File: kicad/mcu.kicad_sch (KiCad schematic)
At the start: 38 parts, among them J301 Debug, J302 Conn_01x03_Pin, Q303 2N7002, SW301 SW_Push, U301 W25Q16JVSS, U302 RP2040, U303 AP22804AW5, Y301 12Mhz

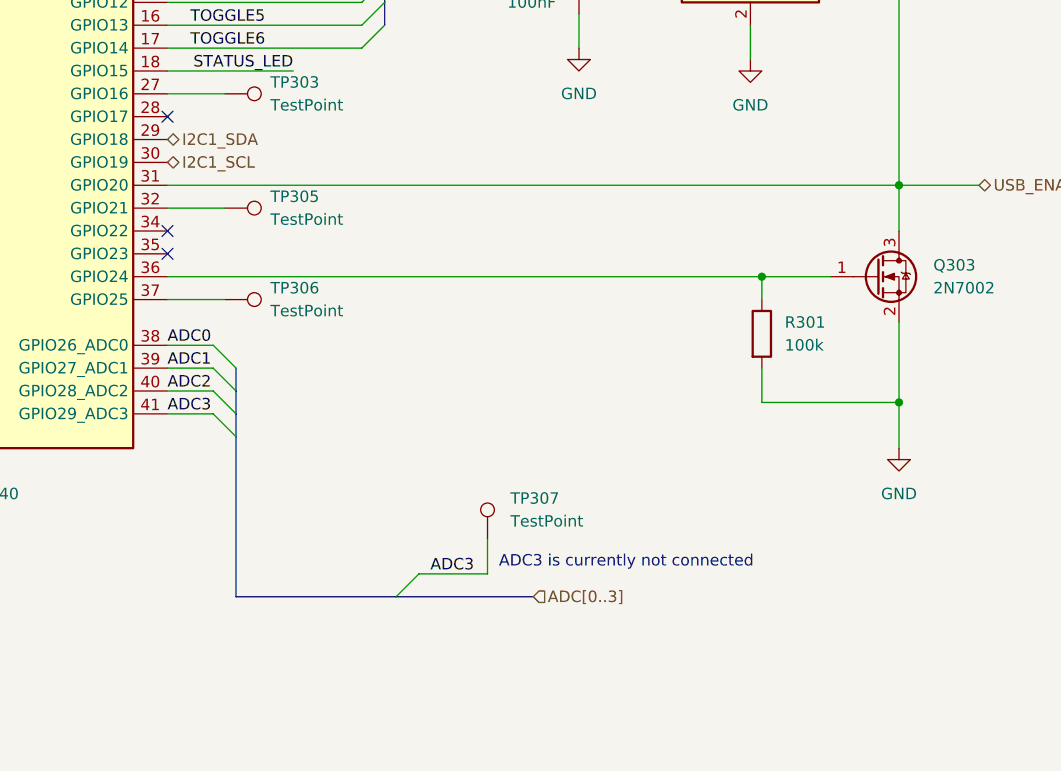
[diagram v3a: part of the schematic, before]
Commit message: Add check for DRC
Only checking errors at the moment, as the board is not ready yet
Moved unconnected Items to severity warning.
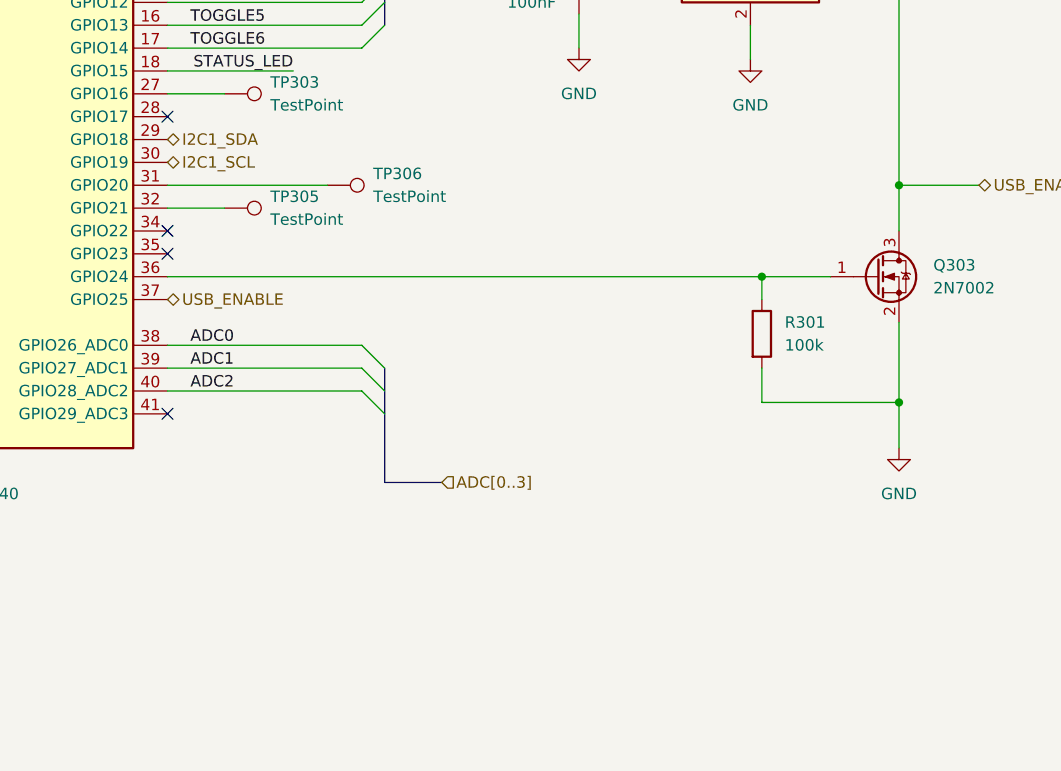
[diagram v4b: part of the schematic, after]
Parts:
- removed TP307: TestPoint, Connector_PinHeader_2.54mm:PinHeader_1x01_P2.54mm_Vertical, symbol Connector:TestPoint
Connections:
- net USB_ENABLE: now also U302.37 (GPIO25); no longer U302.31 (GPIO20)
- net at TP306.1: now also U302.31 (GPIO20); no longer U302.37 (GPIO25)
- net ADC3: no longer names the net of U302.41 (GPIO29_ADC3)
- no-connect marks 7 -> 8
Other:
- note removed: "ADC3 is currently not connected"
- moved on the sheet: TP306
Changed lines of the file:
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@@
 	)
 	(no_connect
+		(at 176.53 132.08)
+	)
+	(no_connect
 		(at 176.53 114.3)
 	)
@@
 	)
 	(bus_entry
-		(at 184.15 129.54)
-		(size -2.54 -2.54)
-		(stroke
-			(width 0)
-			(type default)
-		)
-	)
-	(bus_entry
-		(at 184.15 134.62)
+		(at 200.66 129.54)
 		(size -2.54 -2.54)
 		(stroke
@@
 	)
 	(bus_entry
-		(at 201.93 152.4)
-		(size 2.54 -2.54)
-		(stroke
-			(width 0)
-			(type default)
-		)
-	)
-	(bus_entry
 		(at 200.66 86.36)
 		(size -2.54 2.54)
@@
 	)
 	(bus_entry
-		(at 184.15 132.08)
+		(at 200.66 132.08)
 		(size -2.54 -2.54)
 		(stroke
@@
 	)
 	(bus_entry
-		(at 184.15 127)
+		(at 200.66 127)
 		(size -2.54 -2.54)
 		(stroke
@@
 		)
 	)
-	(bus
-		(pts
-			(xy 201.93 152.4) (xy 217.17 152.4)
-		)
-		(stroke
-			(width 0)
-			(type default)
-		)
-	)
 	(wire
 		(pts
@@
 	(bus
 		(pts
-			(xy 184.15 134.62) (xy 184.15 152.4)
+			(xy 200.66 132.08) (xy 200.66 139.7)
 		)
 		(stroke
@@
 	(wire
 		(pts
-			(xy 212.09 146.05) (xy 212.09 149.86)
+			(xy 257.81 27.94) (xy 257.81 30.48)
 		)
 		(stroke
@@
 	(wire
 		(pts
-			(xy 257.81 27.94) (xy 257.81 30.48)
+			(xy 241.3 88.9) (xy 241.3 92.71)
 		)
 		(stroke
@@
 	(wire
 		(pts
-			(xy 241.3 88.9) (xy 241.3 92.71)
+			(xy 176.53 127) (xy 198.12 127)
 		)
 		(stroke
@@
 	(wire
 		(pts
-			(xy 137.16 27.94) (xy 137.16 31.75)
+			(xy 176.53 106.68) (xy 194.31 106.68)
 		)
 		(stroke
@@
 	(wire
 		(pts
-			(xy 176.53 119.38) (xy 182.88 119.38)
+			(xy 137.16 27.94) (xy 137.16 31.75)
 		)
 		(stroke
@@
 	(bus
 		(pts
-			(xy 184.15 129.54) (xy 184.15 132.08)
+			(xy 200.66 129.54) (xy 200.66 132.08)
 		)
 		(stroke
@@
 	(bus
 		(pts
-			(xy 184.15 152.4) (xy 201.93 152.4)
+			(xy 200.66 139.7) (xy 207.01 139.7)
 		)
 		(stroke
@@
 	(wire
 		(pts
-			(xy 176.53 129.54) (xy 181.61 129.54)
-		)
-		(stroke
-			(width 0)
-			(type default)
-		)
-	)
-	(wire
-		(pts
 			(xy 232.41 20.32) (xy 219.71 20.32)
 		)
@@
 	(wire
 		(pts
+			(xy 176.53 129.54) (xy 198.12 129.54)
+		)
+		(stroke
+			(width 0)
+			(type default)
+		)
+	)
+	(wire
+		(pts
 			(xy 91.44 78.74) (xy 125.73 78.74)
 		)
@@
 	(wire
 		(pts
-			(xy 176.53 132.08) (xy 181.61 132.08)
-		)
-		(stroke
-			(width 0)
-			(type default)
-		)
-	)
-	(wire
-		(pts
 			(xy 270.51 20.32) (xy 270.51 22.86)
 		)
@@
 		)
 	)
-	(wire
+	(bus
 		(pts
-			(xy 176.53 127) (xy 181.61 127)
+			(xy 200.66 127) (xy 200.66 129.54)
 		)
 		(stroke
@@
 		)
 	)
-	(bus
+	(wire
 		(pts
-			(xy 184.15 127) (xy 184.15 129.54)
+			(xy 242.57 116.84) (xy 176.53 116.84)
 		)
 		(stroke
@@
 	(wire
 		(pts
-			(xy 242.57 116.84) (xy 176.53 116.84)
+			(xy 257.81 20.32) (xy 257.81 22.86)
 		)
 		(stroke
@@
 	(wire
 		(pts
-			(xy 257.81 20.32) (xy 257.81 22.86)
+			(xy 36.83 173.99) (xy 44.45 173.99)
 		)
 		(stroke
@@
 	(wire
 		(pts
-			(xy 36.83 173.99) (xy 44.45 173.99)
+			(xy 176.53 124.46) (xy 198.12 124.46)
 		)
 		(stroke
@@
 	(wire
 		(pts
-			(xy 204.47 149.86) (xy 212.09 149.86)
-		)
-		(stroke
-			(width 0)
-			(type default)
-		)
-	)
-	(wire
-		(pts
 			(xy 176.53 86.36) (xy 198.12 86.36)
 		)
@@
 	(wire
 		(pts
-			(xy 181.61 124.46) (xy 176.53 124.46)
-		)
-		(stroke
-			(width 0)
-			(type default)
-		)
-	)
-	(wire
-		(pts
-			(xy 176.53 106.68) (xy 257.81 106.68)
-		)
-		(stroke
-			(width 0)
-			(type default)
-		)
-	)
-	(bus
-		(pts
-			(xy 184.15 132.08) (xy 184.15 134.62)
-		)
-		(stroke
-			(width 0)
-			(type default)
-		)
-	)
-	(wire
-		(pts
 			(xy 91.44 83.82) (xy 125.73 83.82)
 		)
@@
 		)
 	)
-	(text "ADC3 is currently not connected"
-		(exclude_from_sim no)
-		(at 213.36 148.59 0)
-		(effects
-			(font
-				(size 1.27 1.27)
-			)
-			(justify left)
-		)
-	)
 	(label "SWCLK"
 		(at 44.45 173.99 180)
@@
 		)
 	)
-	(label "ADC3"
-		(at 176.53 132.08 0)
-		(fields_autoplaced yes)
-		(effects
-			(font
-				(size 1.27 1.27)
-			)
-			(justify left bottom)
-		)
-	)
 	(label "DEBUG_TX"
 		(at 142.24 176.53 180)
@@
 	)
 	(label "ADC0"
-		(at 176.53 124.46 0)
+		(at 179.07 124.46 0)
 		(fields_autoplaced yes)
 		(effects
@@
 		)
 	)
-	(label "ADC3"
-		(at 205.74 149.86 0)
-		(fields_autoplaced yes)
-		(effects
-			(font
-				(size 1.27 1.27)
-			)
-			(justify left bottom)
-		)
-	)
 	(label "USB_VDD"
 		(at 175.26 19.05 180)
@@
 	)
 	(label "ADC2"
-		(at 176.53 129.54 0)
+		(at 179.07 129.54 0)
 		(fields_autoplaced yes)
 		(effects
@@
 	)
 	(label "ADC1"
-		(at 176.53 127 0)
+		(at 179.07 127 0)
 		(fields_autoplaced yes)
 		(effects
@@
 		)
 	)
+	(hierarchical_label "USB_ENABLE"
+		(shape bidirectional)
+		(at 176.53 119.38 0)
+		(fields_autoplaced yes)
+		(effects
+			(font
+				(size 1.27 1.27)
+			)
+			(justify left)
+		)
+	)
 	(hierarchical_label "ADC[0..3]"
 		(shape input)
-		(at 217.17 152.4 0)
+		(at 207.01 139.7 0)
 		(fields_autoplaced yes)
 		(effects
@@
 	(symbol
 		(lib_id "Connector:TestPoint")
-		(at 182.88 119.38 270)
+		(at 194.31 106.68 270)
 		(unit 1)
 		(exclude_from_sim no)
@@
 		(fields_autoplaced yes)
 		(property "Reference" "TP306"
-			(at 187.96 118.1099 90)
+			(at 199.39 105.4099 90)
 			(effects
 				(font
@@
 		)
 		(property "Value" "TestPoint"
-			(at 187.96 120.6499 90)
+			(at 199.39 107.9499 90)
 			(effects
 				(font
@@
 		)
 		(property "Footprint" "Connector_PinHeader_2.54mm:PinHeader_1x01_P2.54mm_Vertical"
-			(at 182.88 124.46 0)
+			(at 194.31 111.76 0)
 			(effects
 				(font
@@
 		)
 		(property "Datasheet" "~"
-			(at 182.88 124.46 0)
+			(at 194.31 111.76 0)
 			(effects
 				(font
@@
 		)
 		(property "Description" "test point"
-			(at 182.88 119.38 0)
+			(at 194.31 106.68 0)
 			(effects
 				(font
@@
 					(unit 1)
 				)
-			)
-		)
-	)
-	(symbol
-		(lib_id "Connector:TestPoint")
-		(at 212.09 146.05 0)
-		(unit 1)
-		(exclude_from_sim no)
-		(in_bom yes)
-		(on_board yes)
-		(dnp no)
-		(fields_autoplaced yes)
-		(property "Reference" "TP307"
-			(at 214.63 141.4779 0)
-			(effects
-				(font
-					(size 1.27 1.27)
-				)
-				(justify left)
-			)
-		)
-		(property "Value" "TestPoint"
-			(at 214.63 144.0179 0)
-			(effects
-				(font
-					(size 1.27 1.27)
-				)
-				(justify left)
-			)
-		)
-		(property "Footprint" "Connector_PinHeader_2.54mm:PinHeader_1x01_P2.54mm_Vertical"
-			(at 217.17 146.05 0)
-			(effects
-				(font
-					(size 1.27 1.27)
-				)
-				(hide yes)
-			)
-		)
-		(property "Datasheet" "~"
-			(at 217.17 146.05 0)
-			(effects
-				(font
-					(size 1.27 1.27)
-				)
-				(hide yes)
-			)
-		)
-		(property "Description" "test point"
-			(at 212.09 146.05 0)
-			(effects
-				(font
-					(size 1.27 1.27)
-				)
-				(hide yes)
-			)
-		)
-		(pin "1"
-		)
-		(instances
-			(project "usb3-hub"
-				(path "/fa2d0b8b-d66f-4d1f-bda6-9ad6b6242db5/e484743e-481f-4d37-adb3-d786ac2b08fb"
-					(reference "TP307")
-					(unit 1)
-				)

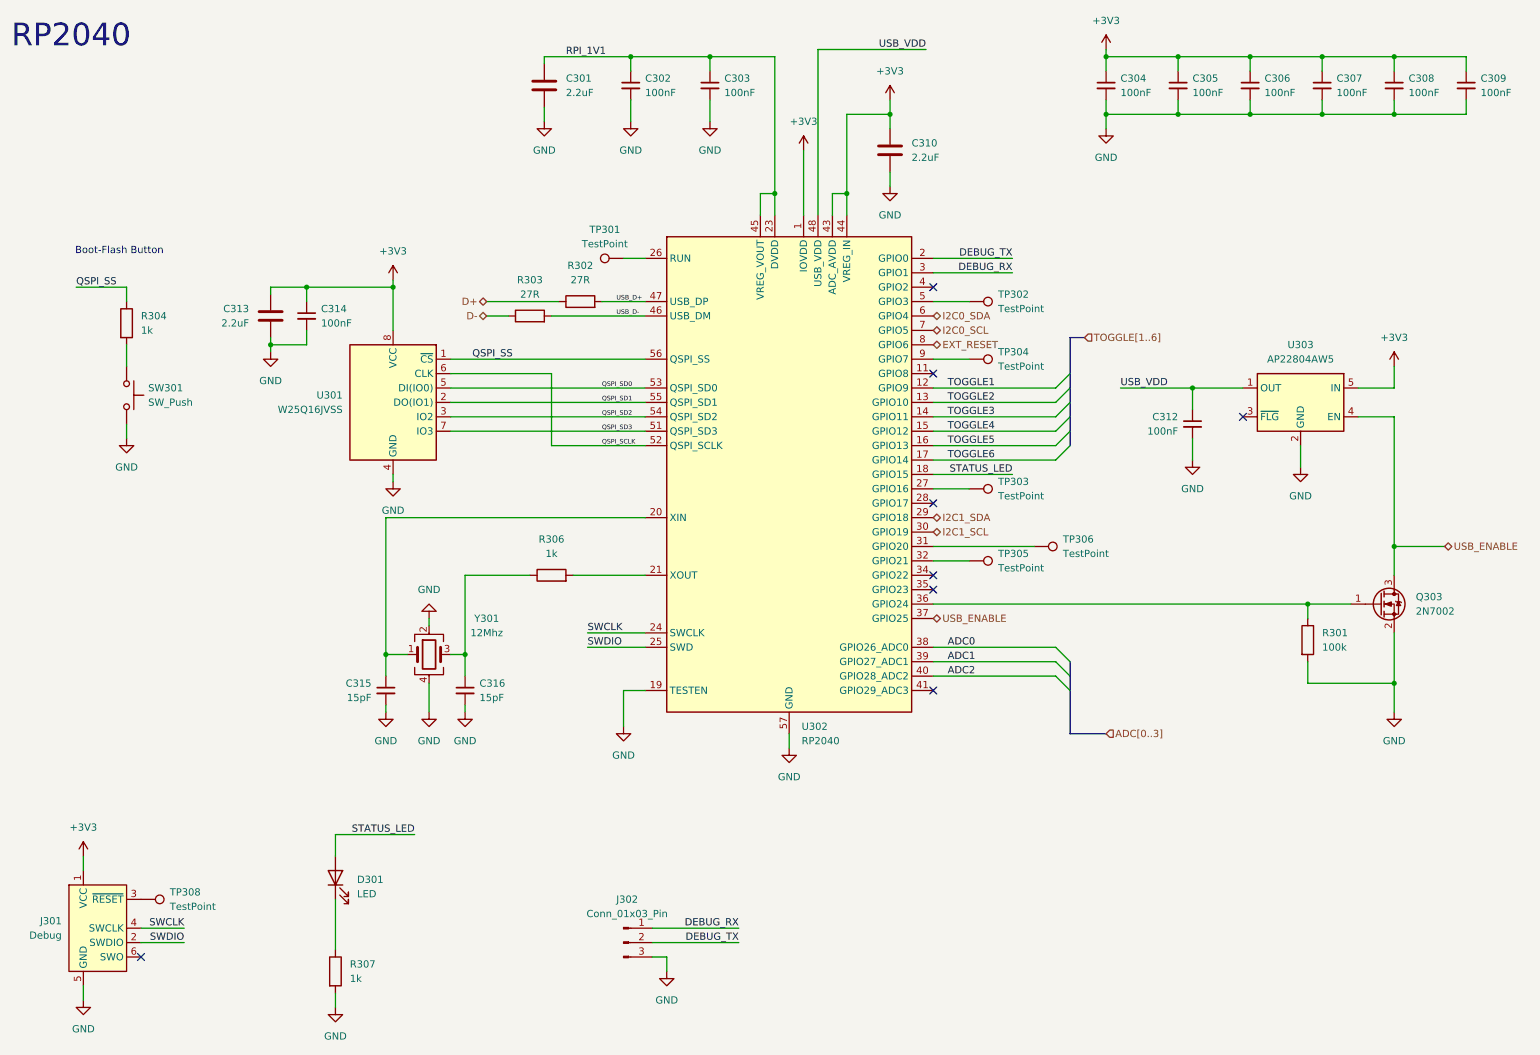
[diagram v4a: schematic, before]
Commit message: Some more routing
rearranged the LED's
Exchanged the testpoints with a 1x5 connector.
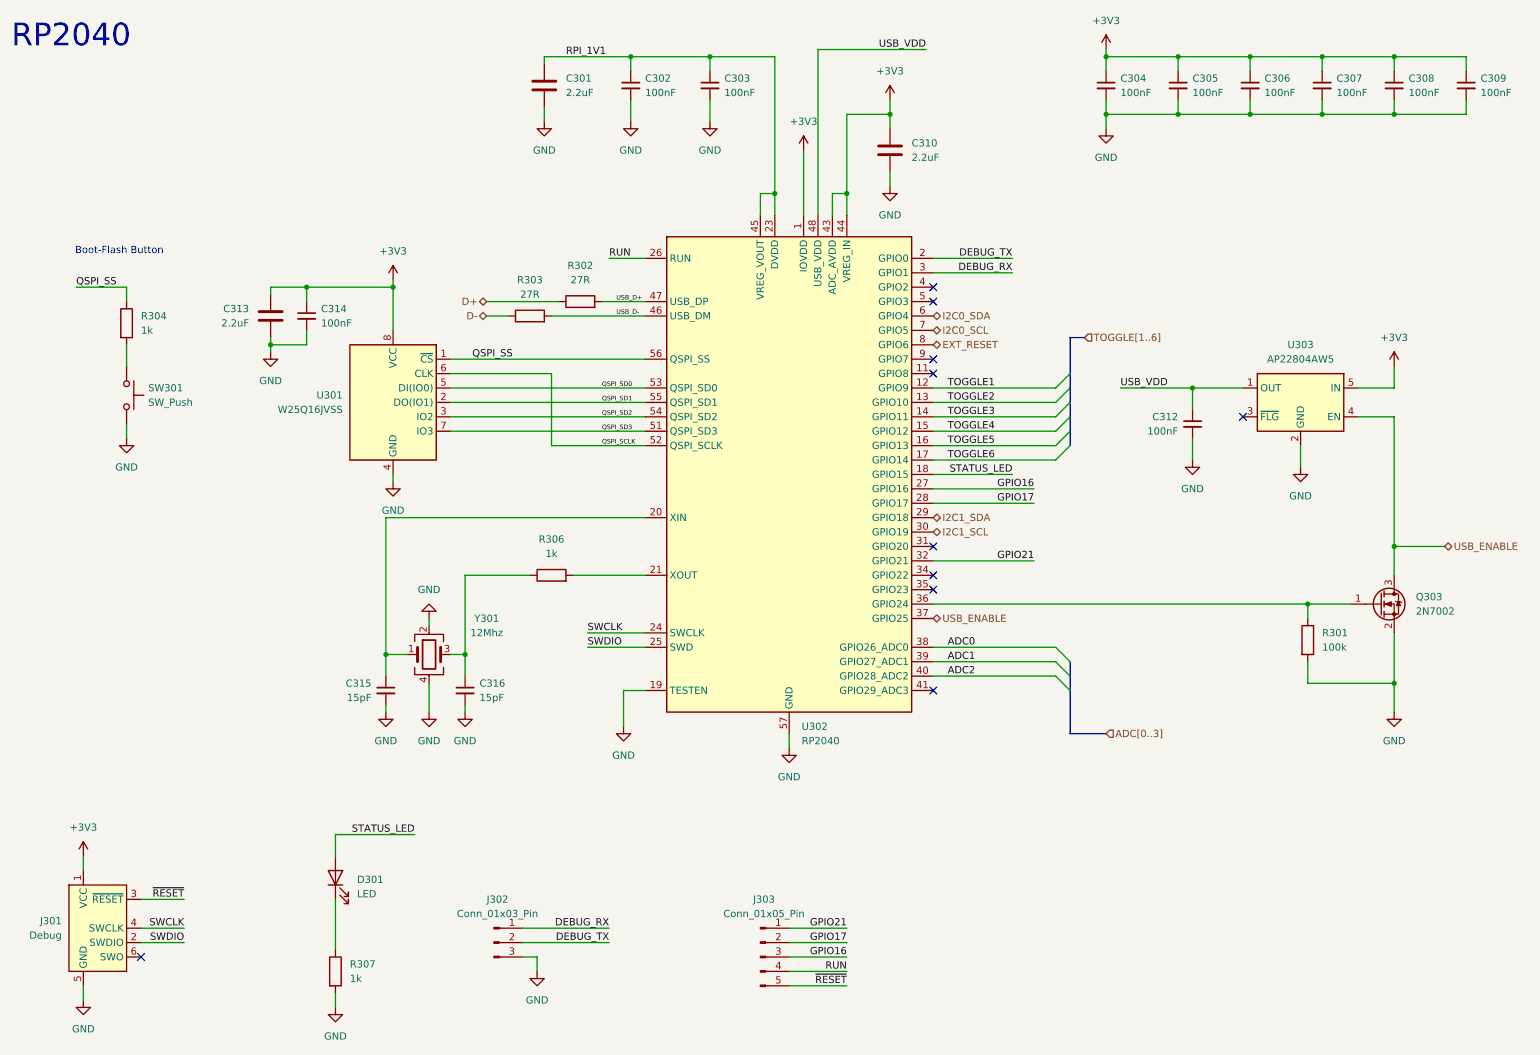
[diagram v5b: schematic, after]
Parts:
- removed TP301, TP302, TP303, TP304, TP305, TP306, TP308: TestPoint, Connector_PinHeader_2.54mm:PinHeader_1x01_P2.54mm_Vertical, symbol Connector:TestPoint
- added J303: Conn_01x05_Pin, Connector_PinSocket_2.54mm:PinSocket_1x05_P2.54mm_Vertical, symbol Connector:Conn_01x05_Pin
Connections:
- net ~{RESET}: now reaches J301.3 (~{RESET})
- net ~{RESET}: now also J303.5 (Pin_5)
- net GPIO16: now reaches U302.27 (GPIO16)
- net GPIO16: now also J303.3 (Pin_3)
- net GPIO21: now reaches U302.32 (GPIO21)
- net GPIO21: now also J303.1 (Pin_1)
- net RUN: now reaches U302.26 (RUN)
- net RUN: now also J303.4 (Pin_4)
- net GPIO17: now reaches U302.28 (GPIO17)
- net GPIO17: now also J303.2 (Pin_2)
- no-connect marks 8 -> 10
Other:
- moved on the sheet: J302
